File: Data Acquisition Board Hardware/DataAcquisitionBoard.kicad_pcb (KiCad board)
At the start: 2 copper layers, 10 parts, among them P1 BNC, P2 BNC, P3 BNC, P4 BNC

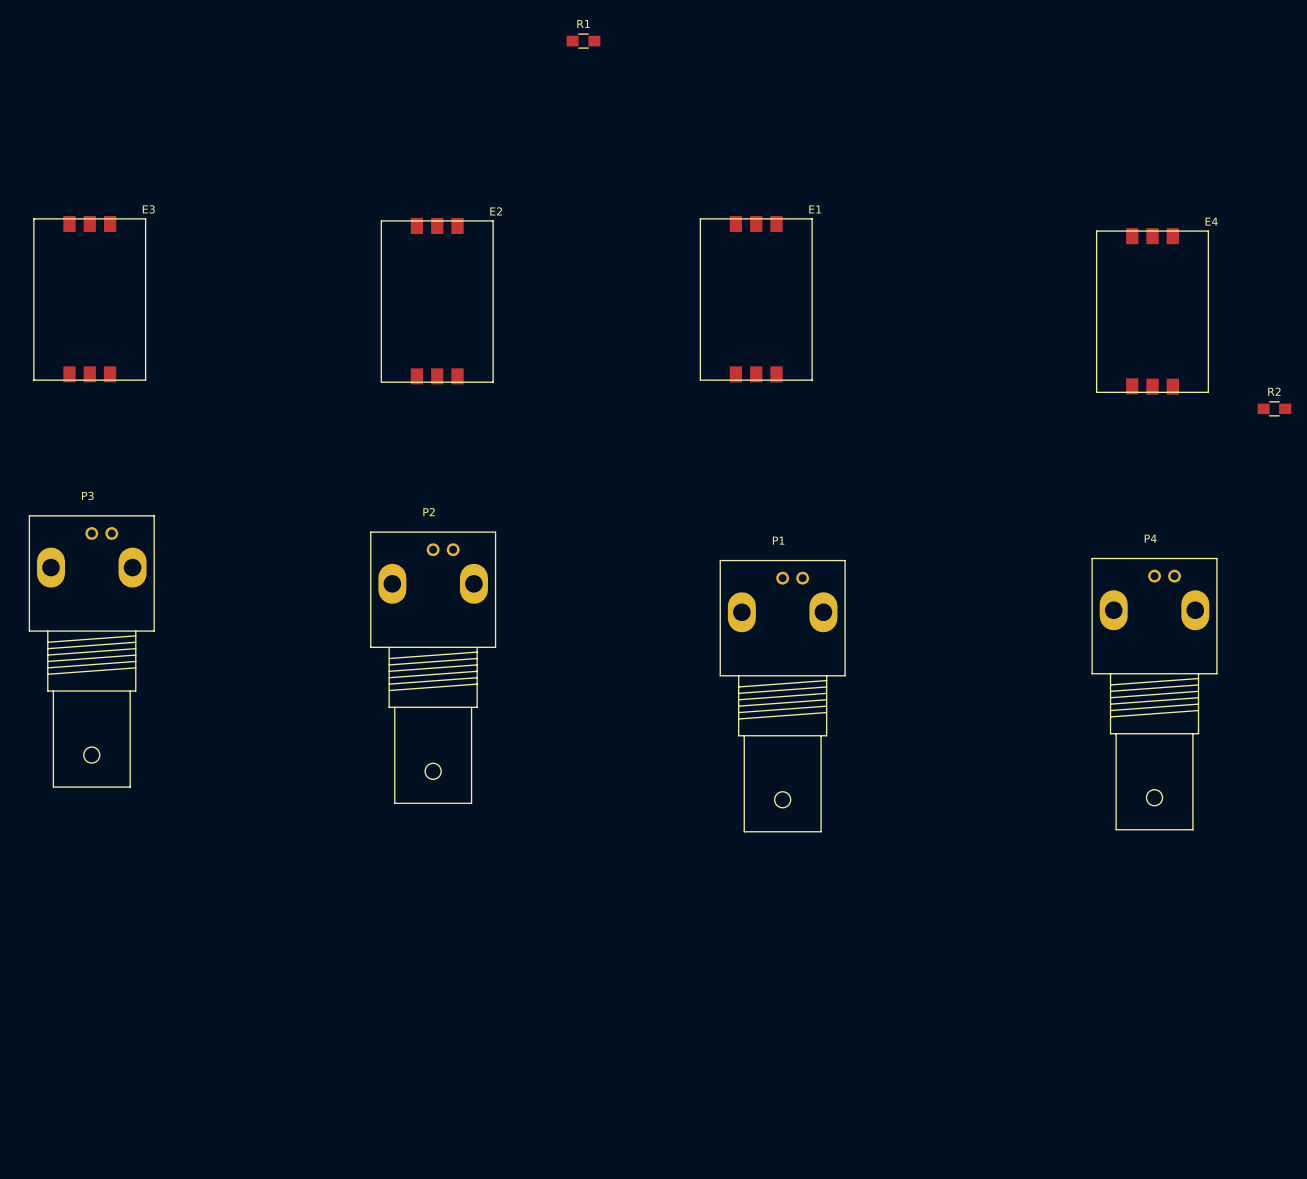
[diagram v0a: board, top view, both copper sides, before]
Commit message: Completed PCB layout, added jumper footprint
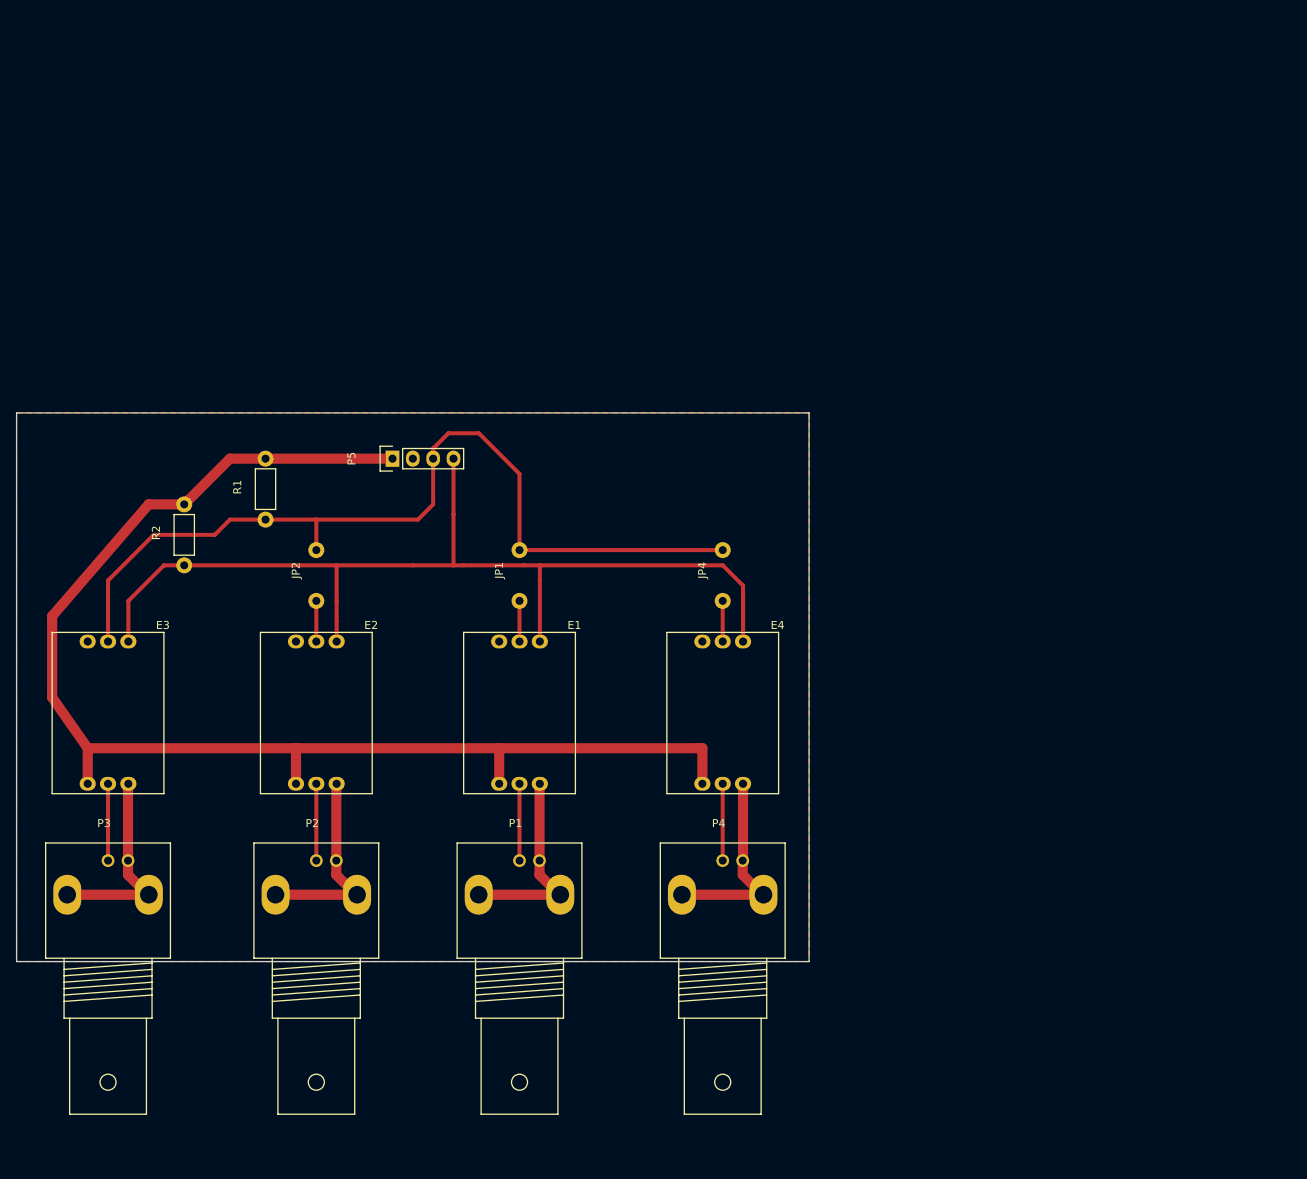
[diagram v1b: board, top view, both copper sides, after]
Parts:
- added JP1: JUMPER, DAB:Jumper_6.35mm, F.Cu at (116.2, 107.3)
- added JP2: JUMPER, DAB:Jumper_6.35mm, F.Cu at (90.8, 107.3)
- added JP4: JUMPER, DAB:Jumper_6.35mm, F.Cu at (141.6, 107.3)
- added P5: CONN_01X04, Pin_Headers:Pin_Header_Straight_1x04, F.Cu at (100.3, 89.5)
- R1, R2: footprint Resistors_SMD:R_0805_HandSoldering -> Resistors_ThroughHole:Resistor_Horizontal_RM7mm
- moved R2 137.7 mm to (74.3, 102.9), turned to 90 degrees
- moved E4 73.5 mm to (141.6, 121.3)
- moved R1 71.8 mm to (84.5, 97.2), turned to 90 degrees
- moved P4 64.6 mm to (141.6, 144.8)
- moved E1 59.6 mm to (116.2, 121.3)
- moved E2 53.6 mm to (90.8, 121.3)
- moved E3 51.7 mm to (64.8, 121.3)
- moved P1 48.3 mm to (116.2, 144.8)
- moved P2 41.5 mm to (90.8, 144.8)
- moved P3 40.9 mm to (64.8, 144.8)
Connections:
- net /5V renamed +5V
- net /A5 renamed A5
- net /Ard_GND renamed GND
- E1 pad 2: /A4 -> Net-(E1-Pad2)
- E2 pad 2: /A4 -> Net-(E2-Pad2)
- E3 pad 2: /A4 -> A4
- E4 pad 2: /A4 -> Net-(E4-Pad2)
- R1 pad 1: /A4 -> A4
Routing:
- net +5V: track 0.00 -> 163.8 mm
- net A5: track 0.00 -> 124.2 mm
- net A4: track 0.00 -> 111.6 mm
- net Net-(E3-Pad4): track 0.00 -> 25.4 mm
- net Net-(E1-Pad4): track 0.00 -> 25.3 mm
- net Net-(E2-Pad4): track 0.00 -> 25.3 mm
- net Net-(E4-Pad4): track 0.00 -> 25.3 mm
- net Net-(E4-Pad5): track 0.00 -> 9.60 mm
- net Net-(E3-Pad5): track 0.00 -> 9.60 mm
- net Net-(E2-Pad5): track 0.00 -> 9.60 mm
- net Net-(E1-Pad5): track 0.00 -> 9.60 mm
- net Net-(E4-Pad2): track 0.00 -> 5.08 mm
- net Net-(E2-Pad2): track 0.00 -> 5.08 mm
- net Net-(E1-Pad2): track 0.00 -> 5.08 mm
- added copper zone on F.Cu, net GND
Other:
- board outline added: 99.1 x 68.6 mm
- net class +5V added: clearance 0.2, trace_width 1.27, via_dia 0.6, via_drill 0.4
- net class Default: trace_width 0.25 -> 0.508
- net class PRBGND added: clearance 0.2, trace_width 1.27, via_dia 0.6, via_drill 0.4
- rule trace_min: 0.2 -> 0.254
- rule via_min_drill: 0.3 -> 0.254
- rule via_min_size: 0.4 -> 0.4064

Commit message: Finalized PCB layout
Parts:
- moved E4 14.3 mm to (154.6, 127.3)
- moved JP4 14.3 mm to (154.6, 113.3)
- moved P4 14.3 mm to (154.6, 150.8)
- moved E1 14.3 mm to (129.2, 127.3)
- moved E2 14.3 mm to (103.8, 127.3)
- moved E3 14.3 mm to (77.8, 127.3)
- moved JP1 14.3 mm to (129.2, 113.3)
- moved JP2 14.3 mm to (103.8, 113.3)
- moved P1 14.3 mm to (129.2, 150.8)
- moved P2 14.3 mm to (103.8, 150.8)
- moved P3 14.3 mm to (77.8, 150.8)
- moved P5 14.3 mm to (113.3, 95.6)
- moved R1 14.3 mm to (97.5, 103.2)
- moved R2 14.3 mm to (87.3, 108.9)
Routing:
- added copper zone on B.Cu, net GND
- removed copper zone on F.Cu, net GND
